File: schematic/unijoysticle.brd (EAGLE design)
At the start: 70.8 x 66 mm, 8 parts, among them CN1 External Battery, IC1 4066N, IC2 4066N, IC3 4066N, X1 Joy #1, X2 Joy #2

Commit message: fix: schematic & board fixed
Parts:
- removed U$1: ESP12E_DEVKIT, ESP12E_DEVKIT:ESP12E_DEVKIT
- added ESP1: ESP12E_DEVKIT, ESP12E_DEVKIT:ESP12E_DEVKIT
- CN1: value External Battery -> 3.3V - 9V
- moved IC2 45.3 mm to (35.6, 44.5)
- moved D1 31.4 mm to (7.62, 16.5)
- moved CN1 28.2 mm to (6.35, -2.54)
- moved IC1 21.0 mm to (12.7, 44.5)
- moved X2 19.1 mm to (52.1, 68.6)
- moved X1 19.0 mm to (20.3, 68.6)
- moved IC3 9.67 mm to (59.7, 44.5)
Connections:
- removed net GNDBREAK: CN1.GNDBREAK
- removed net N$24: D1.C, U$1.VIN
- removed net N$25: CN1.GND, U$1.GND@1
- new net 3.3V: CN1.GND, CN1.GNDBREAK, ESP1.GND@1
- new net 5V: D1.C, ESP1.VIN
- net GND: now also ESP1.GND@3; no longer U$1.GND@3
- net N$1: now also ESP1.D0; no longer U$1.D0
- net N$13: now also IC3.1; no longer IC2.1
- net N$14: now also IC3.4; no longer IC2.4
- net N$15: now also IC3.8; no longer IC2.8
- net N$16: now also IC3.11; no longer IC2.11
- net N$17: now also IC2.2; no longer IC3.2
- net N$18: now also IC3.10, IC3.2, IC3.9; no longer IC2.10, IC2.2, IC2.9
- net N$19: now also ESP1.D4, IC2.13; no longer IC3.13, U$1.D4
- net N$2: now also ESP1.D1; no longer U$1.D1
- net N$20: now also ESP1.RX, IC2.5; no longer IC3.5, U$1.RX
- net N$21: now also IC2.1; no longer IC3.1
- net N$22: now also IC2.4; no longer IC3.4
- net N$3: now also ESP1.D2; no longer U$1.D2
- net N$4: now also ESP1.D3; no longer U$1.D3
- net N$5: now also ESP1.D5, IC3.13; no longer IC2.13, U$1.D5
- net N$6: now also ESP1.D6, IC3.5; no longer IC2.5, U$1.D6
- net N$7: now also ESP1.D7, IC3.6; no longer IC2.6, U$1.D7
- net N$8: now also ESP1.D8, IC3.12; no longer IC2.12, U$1.D8
- net VCC: now also ESP1.3V3@2; no longer U$1.3V3@2
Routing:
- net GND: track 97.7 -> 0.00 mm
- net 3.3V: track 0.00 -> 53.0 mm
- net N$25: track 52.9 -> 0.00 mm
- net 5V: track 0.00 -> 51.6 mm
- net N$24: track 49.5 -> 0.00 mm
- net N$7: track 19.6 -> 41.8 mm
- net N$21: track 27.6 -> 46.1 mm
- net N$8: track 18.7 -> 36.4 mm
- net N$22: track 24.9 -> 38.3 mm
- net N$15: track 20.7 -> 32.8 mm
- net N$9: track 21.8 -> 33.5 mm
- net N$13: track 20.7 -> 32.3 mm
- net VCC: track 92.8 -> 81.1 mm
- net N$14: track 22.6 -> 33.3 mm
- net N$10: track 19.8 -> 29.0 mm
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- added copper zone on layer 1, net GND
- added copper zone on layer 16, net GND
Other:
- board size 70.8 x 66 mm -> 70.8 x 80 mm
- board text added: "RETRO MOE"
- board text added: "REVA"
- board text added: "UniJoystiCle"

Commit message: fix: board fixes
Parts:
- removed ESP1: ESP12E_DEVKIT, ESP12E_DEVKIT:ESP12E_DEVKIT
- added MOD1: NodeMCU Amica v1.0, ESP12E_DEVKIT:ESP12E_DEVKIT
- CN1: value 3.3V - 9V -> DC JACK
- D1: value 1N4004 -> 1N4001
- X1: value Joy #1 -> DSUB 9
- X2: value Joy #2 -> DSUB 9
- moved D1 10.9 mm to (16.5, 22.9), turned to 270 degrees
- moved X1 10.2 mm to (20.3, 58.4)
- moved X2 10.2 mm to (52.1, 58.4)
- moved CN1 5.68 mm to (11.4, 0.00)
- moved IC1 1.80 mm to (14.0, 43.2)
- moved IC2 1.80 mm to (36.8, 43.2)
- moved IC3 1.27 mm to (59.7, 43.2)
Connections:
- net 3.3V: now also MOD1.GND@1; no longer ESP1.GND@1
- net 5V: now also MOD1.VIN; no longer ESP1.VIN
- net GND: now also MOD1.GND@3; no longer ESP1.GND@3
- net N$1: now also MOD1.D0; no longer ESP1.D0
- net N$19: now also MOD1.D4; no longer ESP1.D4
- net N$2: now also MOD1.D1; no longer ESP1.D1
- net N$20: now also MOD1.RX; no longer ESP1.RX
- net N$3: now also MOD1.D2; no longer ESP1.D2
- net N$4: now also MOD1.D3; no longer ESP1.D3
- net N$5: now also MOD1.D5; no longer ESP1.D5
- net N$6: now also MOD1.D6; no longer ESP1.D6
- net N$7: now also MOD1.D7; no longer ESP1.D7
- net N$8: now also MOD1.D8; no longer ESP1.D8
- net VCC: now also MOD1.3V3@2; no longer ESP1.3V3@2
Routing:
- net N$7: track 41.8 -> 20.8 mm
- net N$17: track 62.9 -> 46.4 mm
- net N$18: track 72.7 -> 59.2 mm
- net N$15: track 32.8 -> 20.0 mm, vias 0 -> 1
- net N$13: track 32.3 -> 20.1 mm
- net N$1: track 25.6 -> 37.0 mm
- net N$16: track 21.4 -> 12.2 mm
- net N$9: track 33.5 -> 24.5 mm
- net N$21: track 46.1 -> 37.3 mm
- net N$14: track 33.3 -> 24.6 mm
- net N$22: track 38.3 -> 29.6 mm
- net N$11: track 19.1 -> 10.7 mm
- net N$10: track 29.0 -> 20.7 mm
- net N$6: track 27.6 -> 21.1 mm, vias 1 -> 0
- net VCC: track 81.1 -> 87.3 mm, vias 0 -> 2
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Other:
- board size 70.8 x 80 mm -> 69.5 x 69.8 mm
- board text removed: "RETRO MOE"

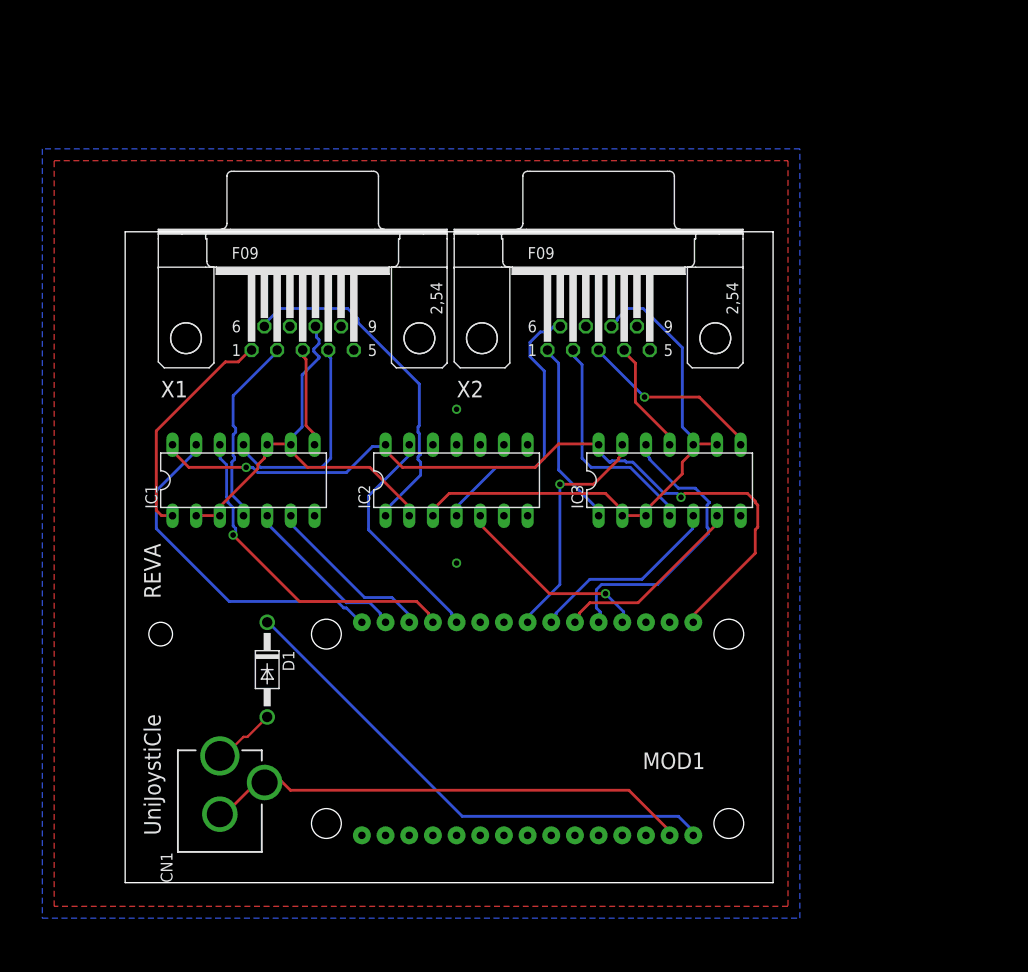
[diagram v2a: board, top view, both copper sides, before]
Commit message: fix: ports in separated by 30.6mm from pin to pin
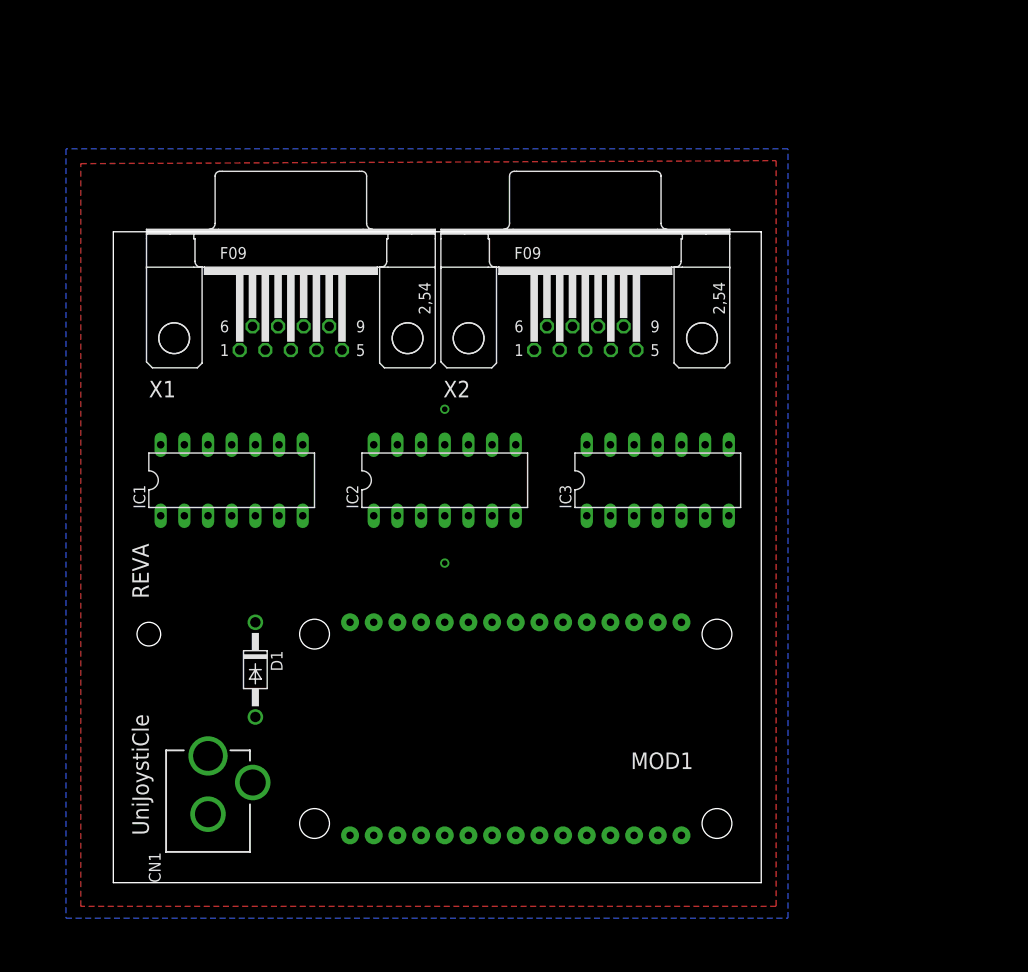
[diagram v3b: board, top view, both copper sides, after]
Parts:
- moved X2 1.43 mm to (50.6, 58.4)
- moved MOD1 1.27 mm to (43.2, 16.5)
- moved D1 1.27 mm to (15.2, 22.9)
- moved IC1 1.27 mm to (12.7, 43.2)
- moved CN1 1.27 mm to (10.2, 0.00)
- moved X1 1.27 mm to (19.1, 58.4)
- moved IC2 1.27 mm to (35.6, 43.2)
- moved IC3 1.27 mm to (58.4, 43.2)
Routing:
- net VCC: track 87.3 -> 0.00 mm, vias 2 -> 0
- net N$18: track 59.2 -> 0.00 mm
- net 5V: track 55.4 -> 0.00 mm
- net 3.3V: track 52.5 -> 0.00 mm
- net N$17: track 46.4 -> 0.00 mm
- net N$21: track 37.3 -> 0.00 mm
- net N$1: track 37.0 -> 0.00 mm
- net N$4: track 36.1 -> 0.00 mm, vias 1 -> 0
- net N$8: track 31.9 -> 0.00 mm
- net N$22: track 29.6 -> 0.00 mm
- net N$5: track 25.5 -> 0.00 mm, vias 1 -> 0
- net N$19: track 24.8 -> 0.00 mm
- net N$14: track 24.6 -> 0.00 mm
- net N$9: track 24.5 -> 0.00 mm
- net N$12: track 22.9 -> 0.00 mm
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
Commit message: fix: new design
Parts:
- removed X1, X2: DSUB 9, con-subd:F09H
- added J1, J2: DB9, SparkFun-Connectors:DB9
- moved CN1 49.5 mm to (59.7, 1.27)
- moved IC1 37.9 mm to (41.9, 19.1)
- moved IC3 36.8 mm to (85.1, 17.8)
- moved D1 32.1 mm to (41.9, 5.08), turned to 0 degrees
- moved MOD1 30.9 mm to (14.0, 26.7), turned to 0 degrees
- moved IC2 30.7 mm to (62.2, 27.9)
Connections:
- net N$10: now also J1.2; no longer X1.2
- net N$11: now also J1.3; no longer X1.3
- net N$12: now also J1.4; no longer X1.4
- net N$13: now also J2.1; no longer X2.1
- net N$14: now also J2.2; no longer X2.2
- net N$15: now also J2.3; no longer X2.3
- net N$16: now also J2.4; no longer X2.4
- net N$17: now also J1.8; no longer X1.8
- net N$18: now also J2.8; no longer X2.8
- net N$21: now also J1.6; no longer X1.6
- net N$22: now also J2.6; no longer X2.6
- net N$9: now also J1.1; no longer X1.1
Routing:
- net GND: track 0.00 -> 100.0 mm
- net VCC: track 0.00 -> 80.0 mm, vias 0 -> 1
- net N$7: track 0.00 -> 78.2 mm
- net N$6: track 0.00 -> 75.1 mm, vias 0 -> 1
- net N$8: track 0.00 -> 72.0 mm
- net 3.3V: track 0.00 -> 69.8 mm
- net N$5: track 0.00 -> 67.7 mm, vias 0 -> 1
- net N$18: track 0.00 -> 66.5 mm
- net N$2: track 0.00 -> 62.4 mm
- net N$17: track 0.00 -> 59.5 mm
- net N$19: track 0.00 -> 47.8 mm
- net N$3: track 0.00 -> 43.8 mm, vias 0 -> 1
- net N$20: track 0.00 -> 42.6 mm
- net 5V: track 0.00 -> 38.2 mm
- net N$14: track 0.00 -> 32.4 mm
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- removed copper zone on layer 1, net GND
- removed copper zone on layer 16, net GND
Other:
- board size 69.5 x 69.8 mm -> 96.2 x 48.2 mm
- board text added: "UniJoystiCle REV 0.2"
- board text added: "http://retro.moe"
- board text removed: "REVA"
- board text removed: "UniJoystiCle"

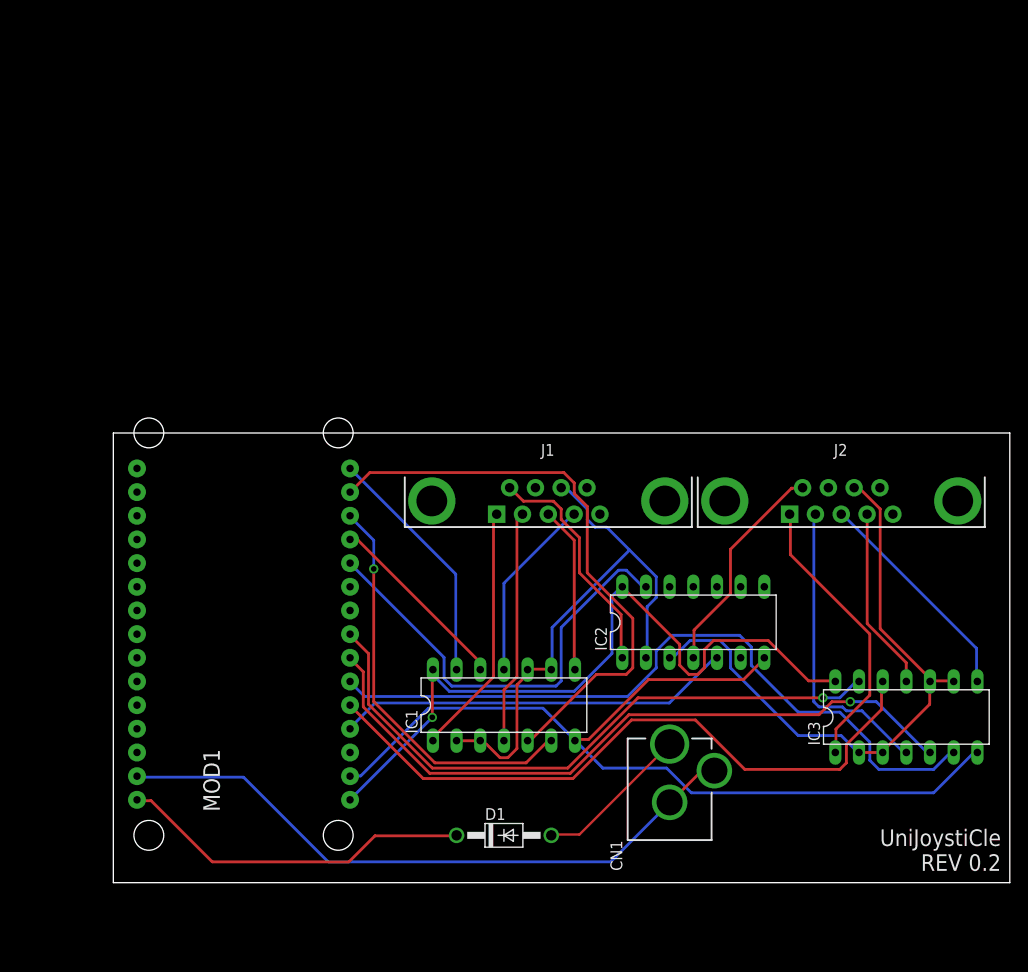
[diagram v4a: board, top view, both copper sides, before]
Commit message: fix: yet another pcb version. smaller, better design
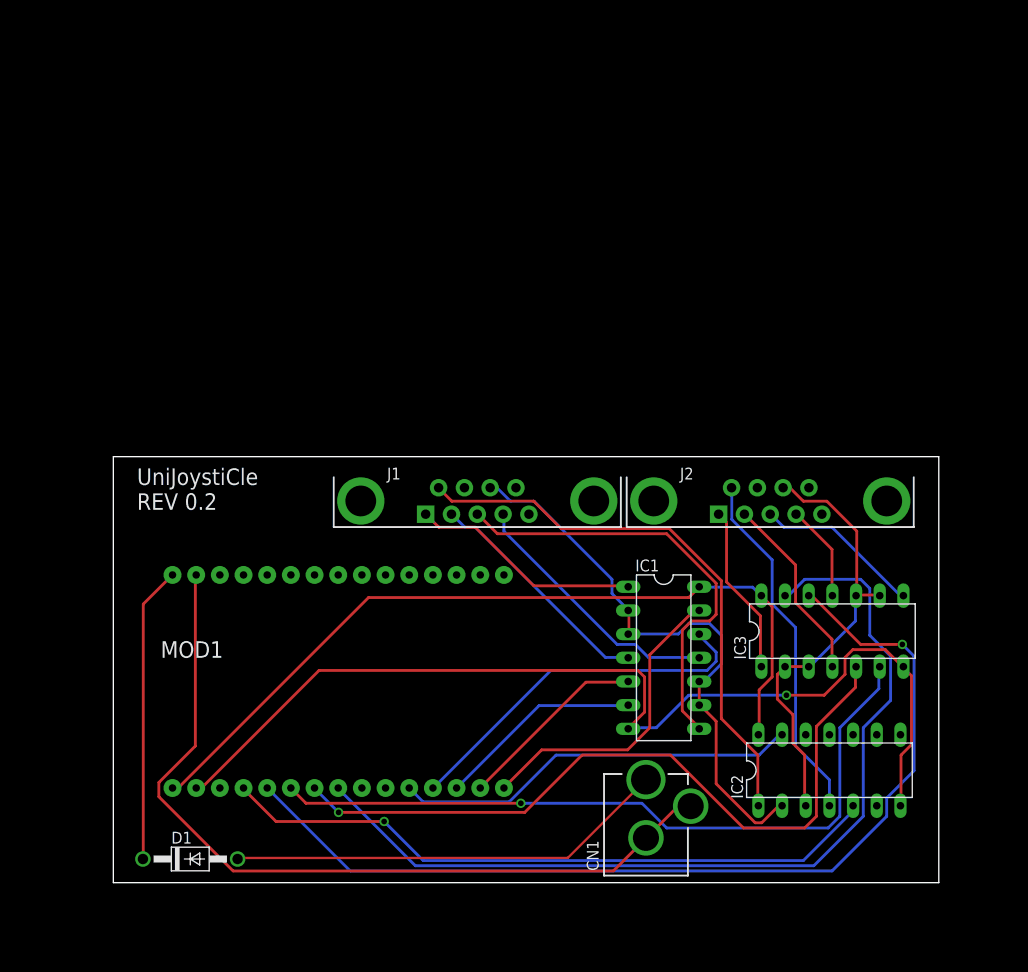
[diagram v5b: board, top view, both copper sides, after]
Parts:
- MOD1: value NodeMCU Amica v1.0 -> ESP12E_DEVKIT
- moved D1 33.8 mm to (8.26, 2.54)
- moved IC2 21.6 mm to (76.8, 12.1)
- moved IC1 17.9 mm to (59.1, 24.1), turned to 270 degrees
- moved IC3 12.2 mm to (77.2, 27.0)
- moved MOD1 11.4 mm to (24.1, 21.6), turned to 270 degrees
- moved J2 7.62 mm to (70.5, 41.0)
- moved J1 7.62 mm to (39.1, 41.0)
- moved CN1 4.58 mm to (57.1, -2.54)
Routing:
- net N$2: track 62.4 -> 20.6 mm
- net N$21: track 25.2 -> 60.3 mm
- net N$8: track 72.0 -> 105.0 mm, vias 0 -> 1
- net N$5: track 67.7 -> 98.9 mm, vias 1 -> 0
- net N$23: track 16.8 -> 47.4 mm
- net N$11: track 17.9 -> 47.7 mm
- net N$20: track 42.6 -> 71.4 mm, vias 0 -> 1
- net N$3: track 43.8 -> 22.1 mm, vias 1 -> 0
- net N$4: track 20.3 -> 39.7 mm
- net 3.3V: track 69.8 -> 88.7 mm
- net N$18: track 66.5 -> 48.2 mm
- net N$22: track 23.8 -> 38.5 mm
- net N$13: track 30.7 -> 18.3 mm
- net N$14: track 32.4 -> 20.3 mm
- net GND: track 100.0 -> 110.5 mm, vias 0 -> 1
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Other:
- board size 96.2 x 48.2 mm -> 88.6 x 45.7 mm
- board text added: "Instructions: http://retro.moe"
- board text removed: "http://retro.moe"

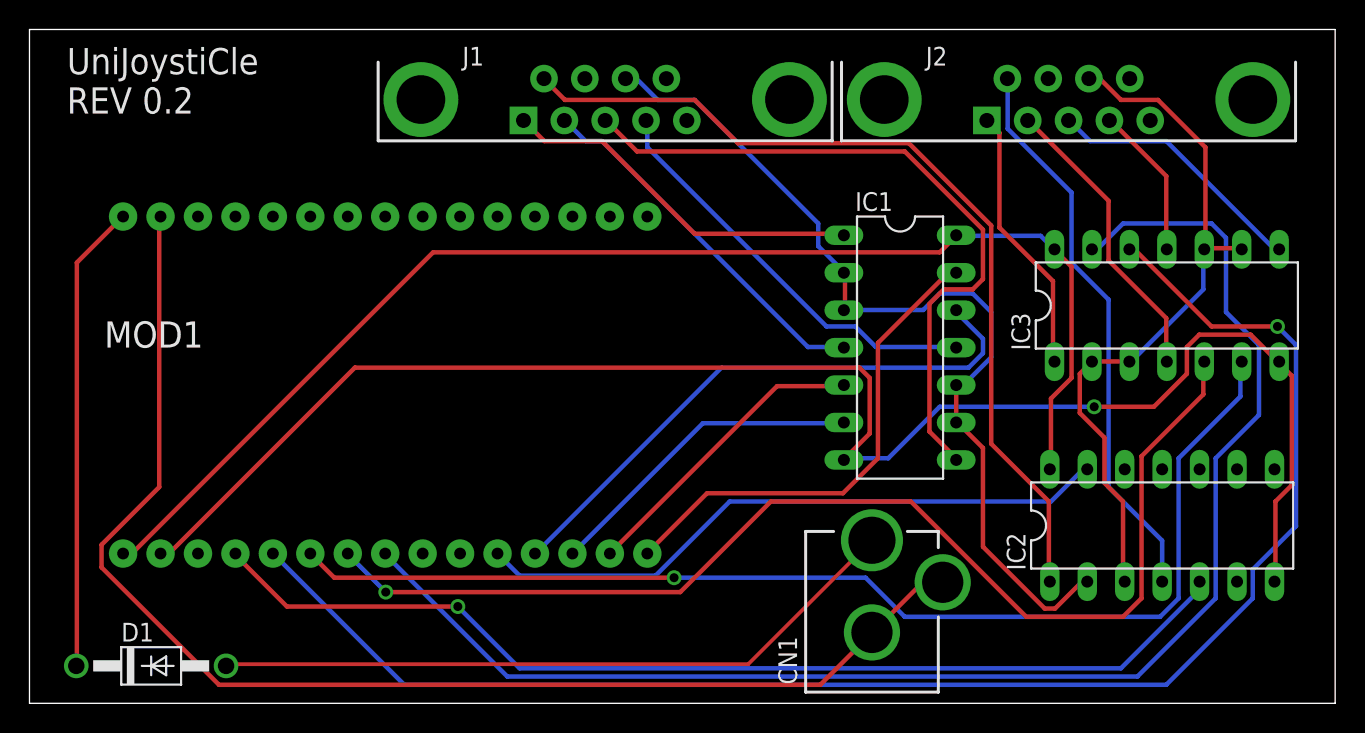
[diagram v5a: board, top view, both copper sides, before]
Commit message: fix: adds .cam file to generate gerbert files
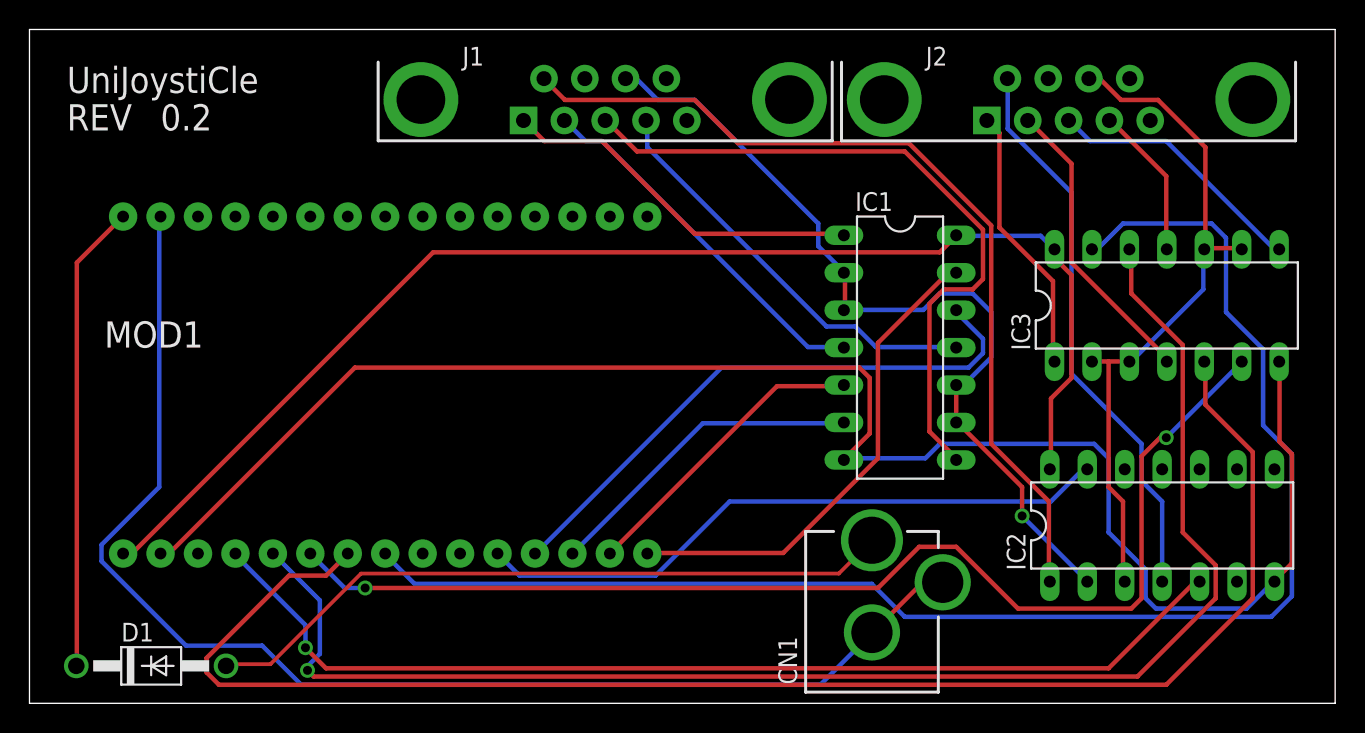
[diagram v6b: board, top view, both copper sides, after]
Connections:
- net N$1 renamed J1UP
- net N$19 renamed J1FIRE
- net N$2 renamed J1DOWN
- net N$20 renamed J2FIRE
- net N$3 renamed J1LEFT
- net N$4 renamed J1RIGHT
- net N$5 renamed J2UP
- net N$6 renamed J2DOWN
- net N$7 renamed J2LEFT
- net N$8 renamed J2RIGHT
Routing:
- net J2DOWN: track 79.1 -> 104.6 mm, vias 1 -> 0
- net J2RIGHT: track 105.0 -> 99.7 mm
- net N$17: track 62.4 -> 58.1 mm, vias 0 -> 1
- net GND: track 110.5 -> 114.8 mm, vias 1 -> 0
- net J2UP: track 98.9 -> 100.3 mm
- net N$18: track 48.2 -> 47.1 mm
- net J2LEFT: track 79.0 -> 79.6 mm, vias 1 -> 2
- net J2FIRE: track 71.4 -> 72.0 mm
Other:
- board text added: ">REVISION"
- board text added: "REV"
- board text added: "UniJoystiCle"
- board text removed: "UniJoystiCle REV 0.2"
